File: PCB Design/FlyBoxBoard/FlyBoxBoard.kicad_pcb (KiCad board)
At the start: 2 copper layers, 148.6 x 119.4 mm, 45 parts, among them J1 5V in, J10 RED, J11 GREEN, J12 WHITE, J13 INFRARED, J14 LCD Screen, J15 SD card reader, J16 5KΩ, J17 5KΩ, J18 ESP 32 unused pins, J19 ESP 32 Left Side extra pinouts, J2 12V in, J20 Transistor, J21 Logic Level LV pins, J22 Potentiometer, J23 Logic Level Left Side LV, J24 GND, J25 ESP 32 unused pins, J26 BuckPuck IR, J27 Logic Level Right Side HV, J28 Logic Level HV pins, J29 5KΩ, J3 ESP 32 Left Side, J30 5KΩ, J31 5KΩ, J32 5KΩ, J33 5KΩ, J34 5KΩ, J35 Transistor, J36 Transistor, J37 Transistor, J38 BuckPuck White, J39 BuckPuck Green, J4 Real Time Controller, J40 BuckPuck Red, J5 ESP 32 Right Side, J6 Rotary Knob, J7 5V, J8 12V, J9 FANS

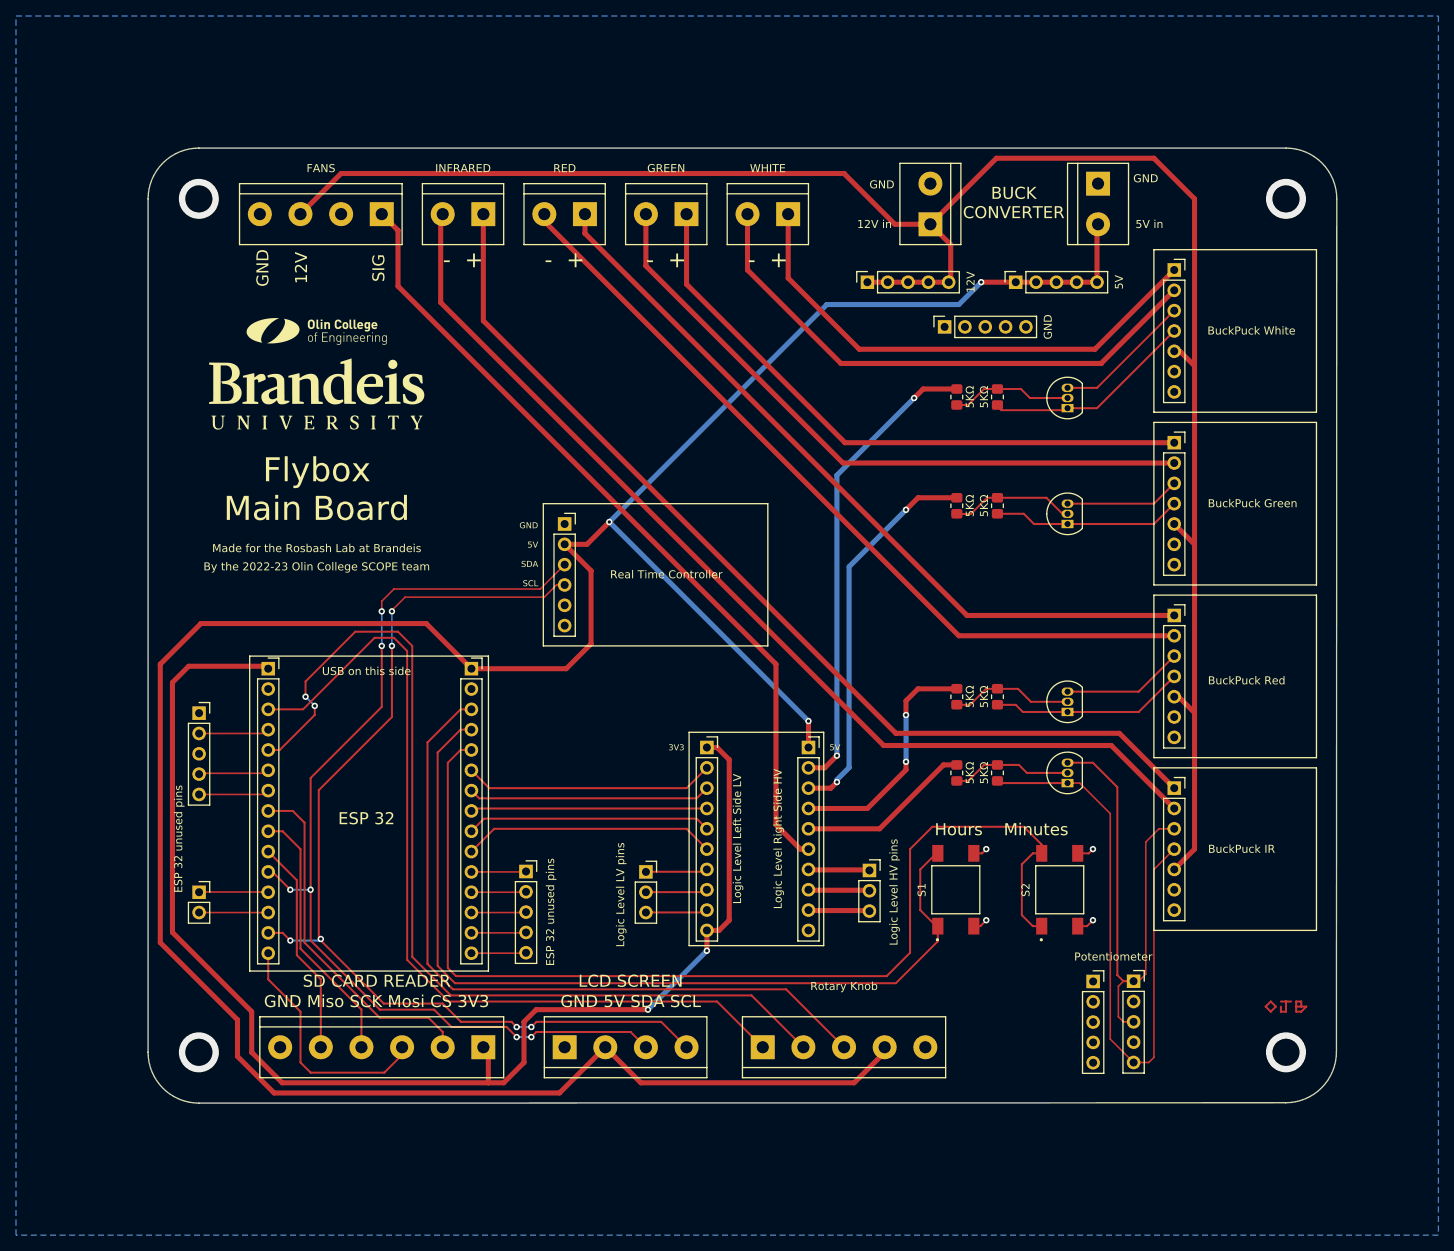
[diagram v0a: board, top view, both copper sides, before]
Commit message: A few more PCB edits
- Eliminated and/or shortened traces on rear side (no more long traces on the rear side)
- Connected four screw vias on IR board to GND
- Ran DRC on all boards and addressed issues where necessary

Imo, we should be ready to order on @oliviajobradley's approval.
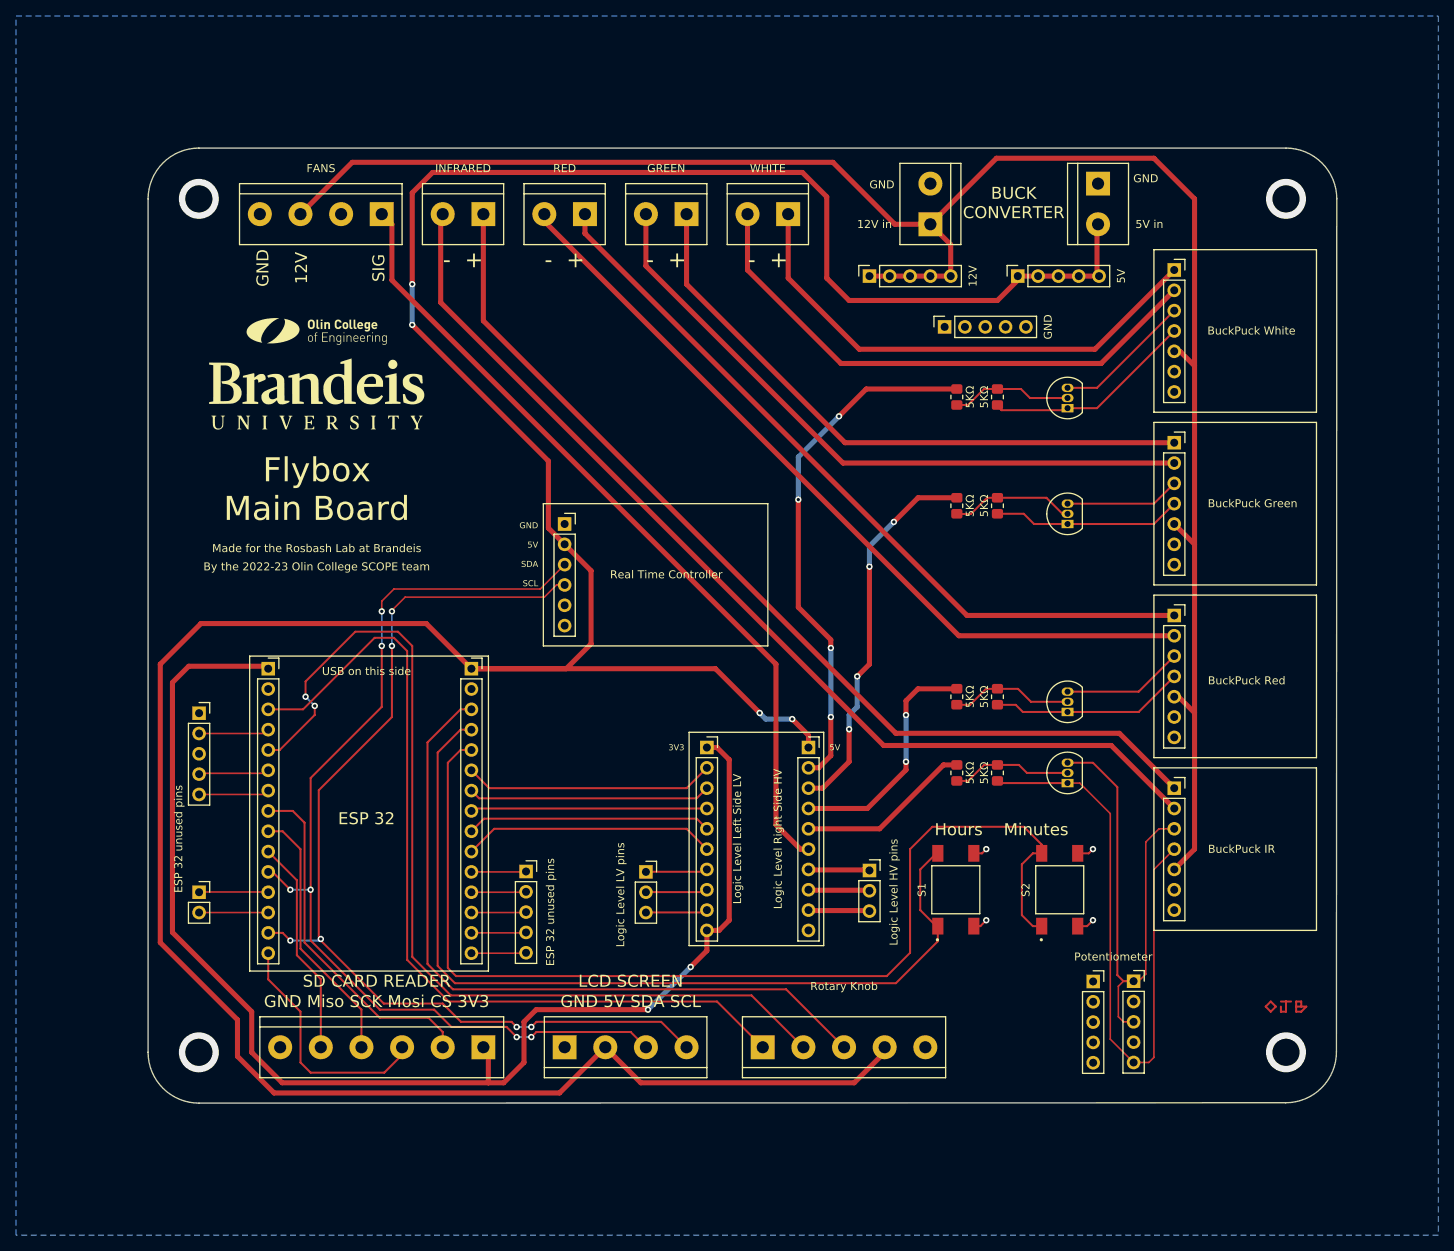
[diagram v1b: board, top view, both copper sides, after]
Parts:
- moved J8 0.80 mm to (106.7, 32.5)
- moved J7 0.80 mm to (125.2, 32.5)
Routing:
- net /5V: track 341.5 -> 422.2 mm, vias 3 -> 4
- net /HV1: track 58.7 -> 65.8 mm, vias 2 -> 4
- net /HV2: track 48.5 -> 47.9 mm, vias 2 -> 4

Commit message: Version 3 Assembly Edits
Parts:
- moved G*** 29.2 mm to (64.8, 49.5)
- moved J6 4.45 mm to (97.8, 128.9)
- moved J1 3.18 mm to (138.4, 21.0)
- moved J14 2.54 mm to (71.1, 128.9)
- moved J25 1.65 mm to (65.4, 106.9)
- moved G*** 1.53 mm to (37.5, 48.9)
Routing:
- net (no net): track 12.7 -> 0.00 mm
- net /5V: track 422.2 -> 428.4 mm
- net /D15: track 109.3 -> 114.2 mm
- net /D4: track 121.4 -> 125.8 mm
- net /D13: track 91.3 -> 95.7 mm
- net /3V3: track 165.6 -> 169.2 mm
- net /D22: track 126.9 -> 129.8 mm
- net /D21: track 125.0 -> 127.6 mm
- net Net-(J25-Pad4): track 6.85 -> 8.50 mm
- net Net-(J25-Pad2): track 6.85 -> 8.50 mm
- net Net-(J25-Pad5): track 6.85 -> 8.50 mm
- net Net-(J25-Pad3): track 6.85 -> 8.50 mm
- net Net-(J25-Pad1): track 6.85 -> 8.50 mm
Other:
- board text added: "3.3V GND D15 D2 D4 RX2 TX2 D5 D18 D19 D21 RX0 TX0 D22 D23"
- board text added: "CLK DT SW + (5V) GND"
- board text added: "ESP-WROOM-32"
- board text added: "GND 12V RPM SIG PWM SIG"
- board text added: "GND 5V SDA SCL SQW 32K"
- board text added: "LCD Screen"
- board text added: "Olivia Jo Bradley"
- board text added: "SD Card Reader"
- board text added: "VIN GND D13 D12 D14 D27 D26 D25 D33 D32 D35 D34 VN VP EN"
- board text removed: "ESP 32"
- board text removed: "GND 12V SIG"
- board text removed: "LCD SCREEN"
- board text removed: "SD CARD READER"

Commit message: Fixed capitalization
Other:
- board text added: "FlyBox Main Board"
- board text removed: "Flybox Main Board"
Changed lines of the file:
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@@
     (effects (font (size 2 2) (thickness 0.3)))
   )
-  (gr_text "Flybox\nMain Board\n" (at 37.592 59.182) (layer "F.SilkS")
+  (gr_text "FlyBox\nMain Board\n" (at 37.592 59.182) (layer "F.SilkS")
     (effects (font (size 3 3) (thickness 0.3)))
   )

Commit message: Zachary final review of PCBs
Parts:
- moved G*** 25.4 mm to (39.6, 46.2)
- moved G*** 5.74 mm to (39.9, 54.1)
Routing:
- net /5V: track 428.4 -> 429.5 mm
- net /D21: track 127.6 -> 128.2 mm
